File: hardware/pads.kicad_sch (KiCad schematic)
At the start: 57 parts, among them J1 5V, J10 5V, J11 5V, J12 5V, J13 5V, J14 5V, J15 5V, J16 5V, J17 5V, J18 5V, J19 5V, J2 5V, J20 5V, J21 5V, J22 5V, J23 5V, J24 5V, J25 5V, J26 5V, J27 5V, J28 5V, J29 5V, J3 5V, J30 5V, J31 5V, J32 5V, J33 5V, J34 5V, J35 5V, J36 5V, J37 5V, J38 5V, J39 5V, J4 5V, J40 5V, J41 5V, J42 5V, J43 5V, J44 5V, J45 5V, J46 5V, J47 5V, J48 5V, J49 5V, J5 5V, J50 5V, J51 5V, J52 5V, J53 5V, J54 5V, J55 5V, J6 5V, J7 5V, J8 5V, J9 5V, P1 SM08B-SRSS-TB(LF)(SN), U8 SM06B-SRSS-TB(LF)(SN)

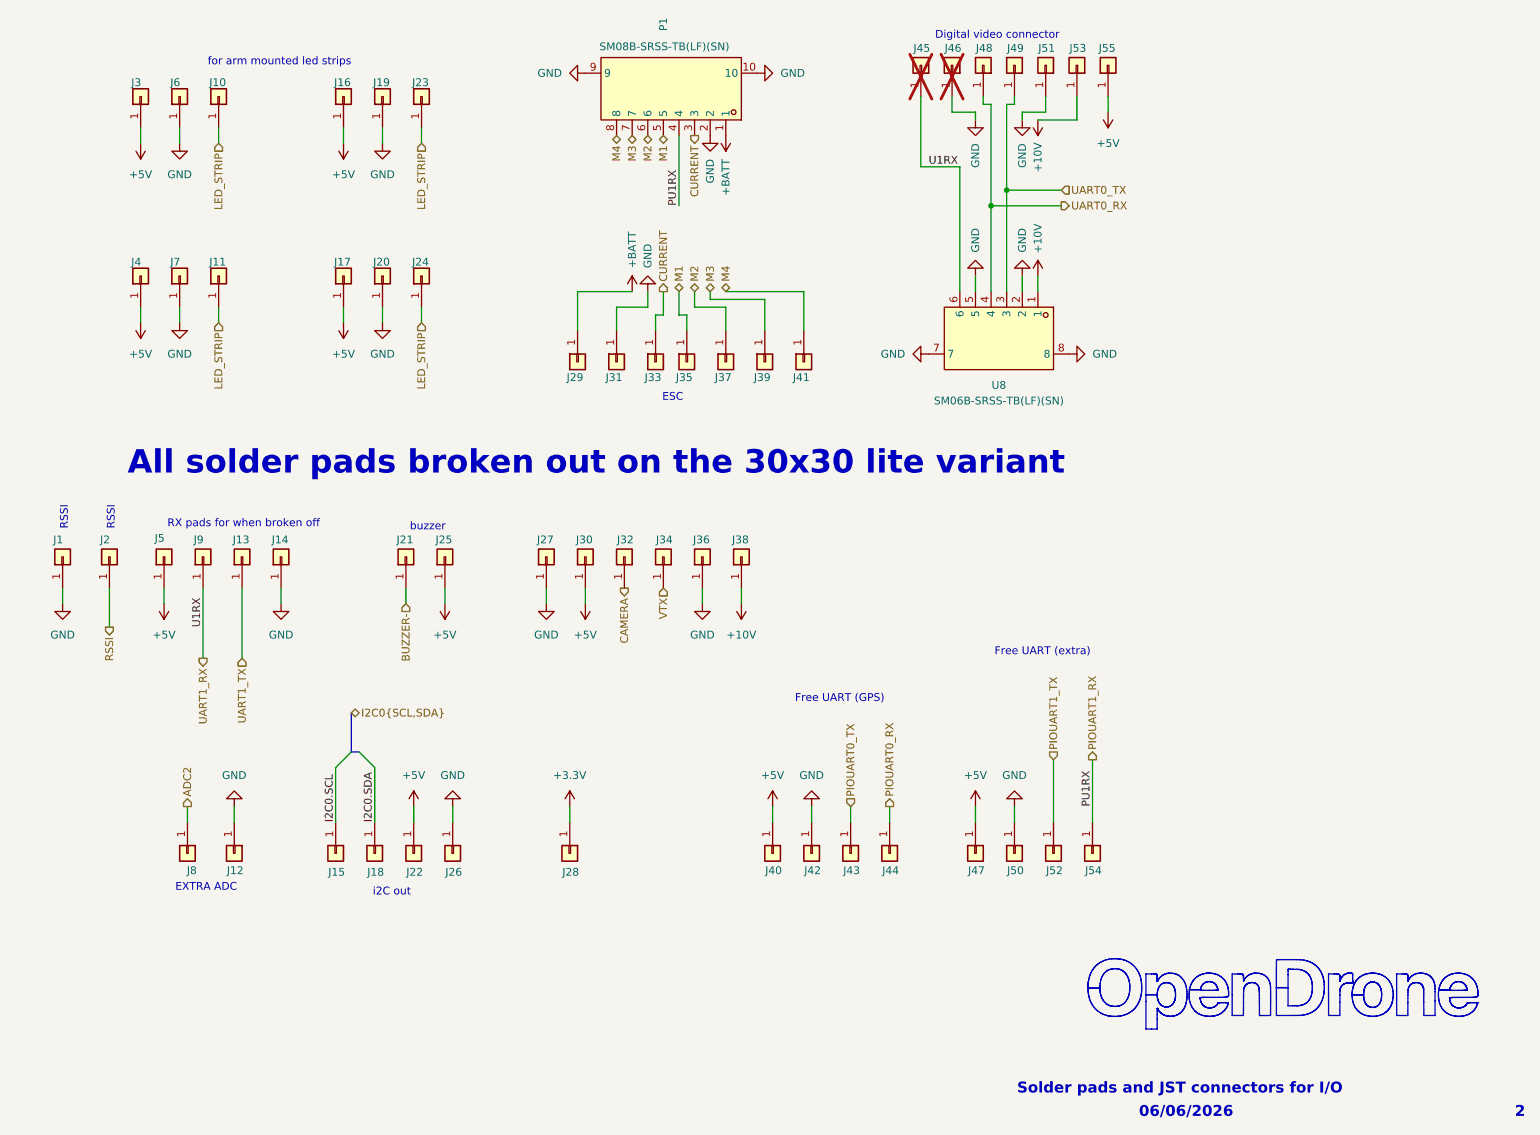
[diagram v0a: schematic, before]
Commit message: Re-route with connectors
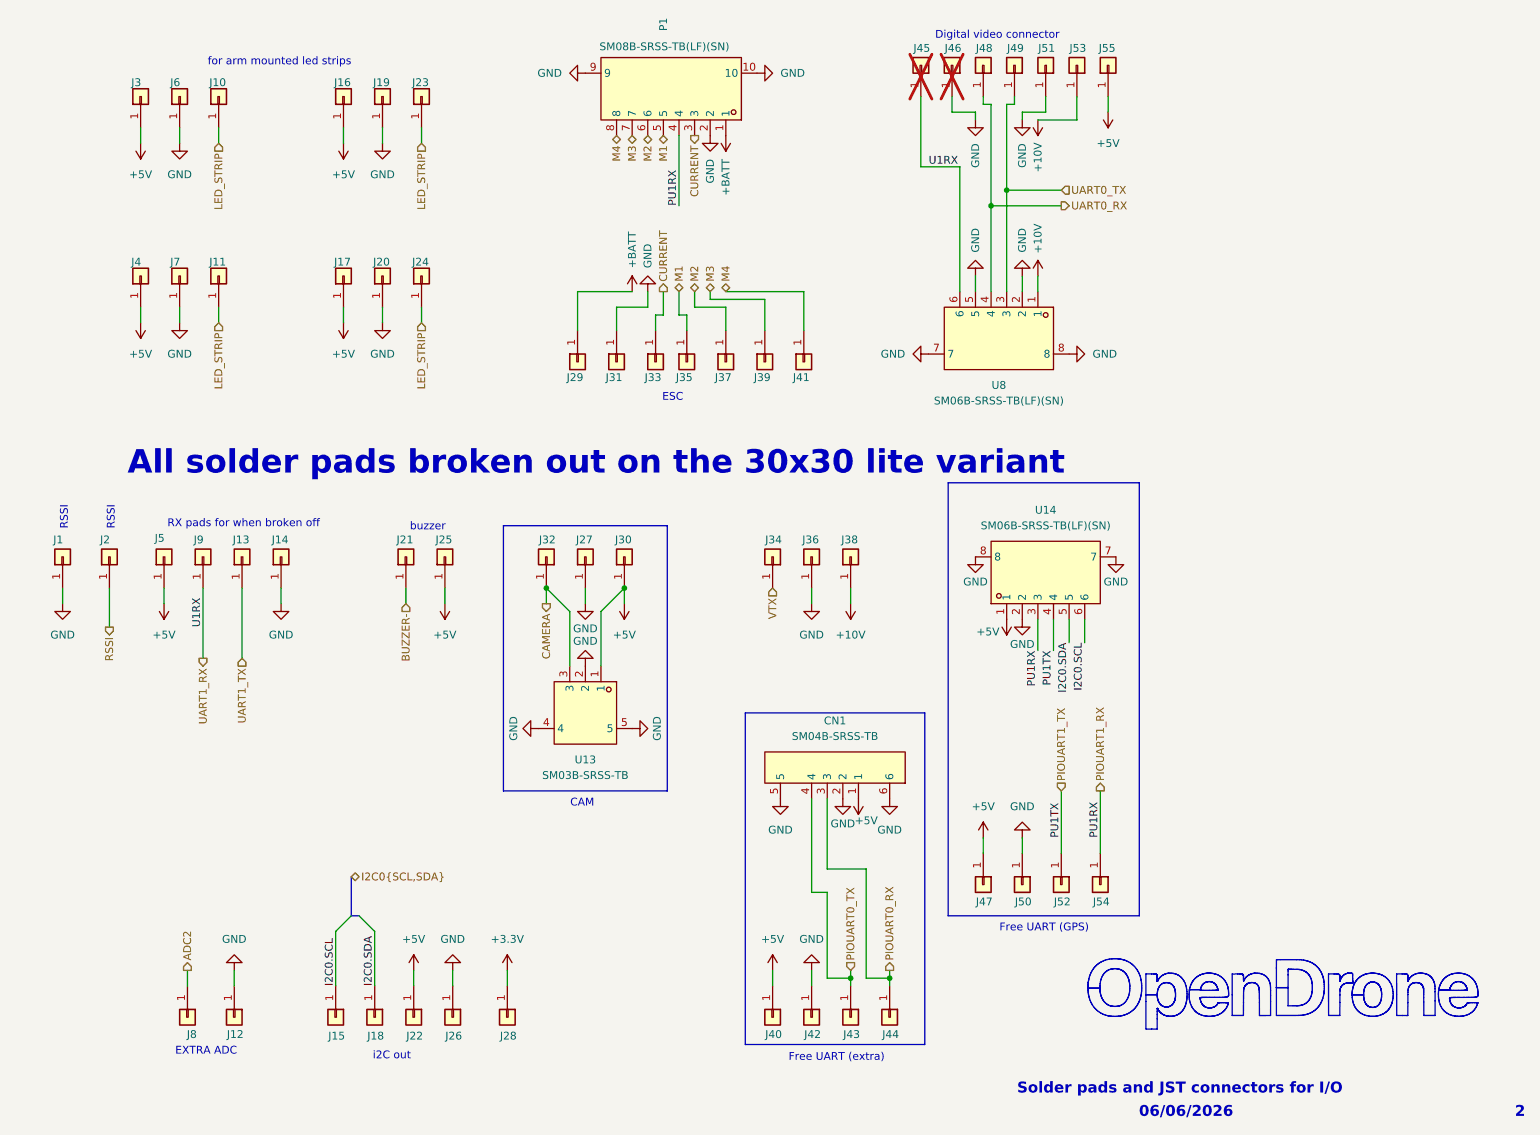
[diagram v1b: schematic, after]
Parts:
- added CN1: SM04B-SRSS-TB, lib:CONN-SMD_4P-P1.00_SM04B-SRSS-TB-LF-SN, symbol lib:SM04B-SRSS-TB
- added U13: SM03B-SRSS-TB, lib:CONN-SMD_SM03B-SRSS-TB-LF-SN-P, symbol lib:SM03B-SRSS-TB
- added U14: SM06B-SRSS-TB(LF)(SN), lib:CONN-SMD_SM06B-SRSS-TB-LF-SN, symbol lib:SM06B-SRSS-TB(LF)(SN)
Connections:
- net +5V: now also CN1.1, U13.1, U14.1
- net CAMERA: now also U13.3
- net GND: now also CN1.2, CN1.5, CN1.6, U13.2, U13.4, U13.5, U14.2, U14.7, U14.8
- net I2C0.SCL: now also U14.6
- net I2C0.SDA: now also U14.5
- net PIOUART0_RX: now also CN1.3
- net PIOUART0_TX: now also CN1.4
- net PIOUART1_RX: now also U14.3
- net PIOUART1_TX: now also U14.4
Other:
- note added: "CAM"
- moved on the sheet: J12, J15, J18, J22, J26, J27, J28, J30, J32, J34, J36, J38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
